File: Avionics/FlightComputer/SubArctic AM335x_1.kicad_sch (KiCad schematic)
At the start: 1 part

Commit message: Ian Goldberg - Made substantial additions to the main chip of the flight computer. Wrapping up progress for the night.
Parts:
- added R169, R170, R171, R172, R173, R35, R43, R44, R7, R9: 33R,5%, symbol Device:R
- renumbered U2 to SubArcticAM335X
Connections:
- new net MMC1_CLK: R35.2
- new net MMC1_CMD: R7.2
- new net MMC1_DAT0: R43.2
- new net MMC1_DAT1: R44.2
- new net MMC1_DAT2: R9.2
- new net MMC1_DAT3: R169.2
- new net MMC1_DAT4: R170.2
- new net MMC1_DAT5: R171.2, R172.2
- new net MMC1_DAT6: R173.2
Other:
- note added: "Are these terminated?"
- note added: "JTAG_TRSTn JTAG_TMS JTAG_TDI JTAG_TCK JTAG_TDO JTAG_EMU0 JTAG_EMU1"
- note added: "SubArctic AM335x"

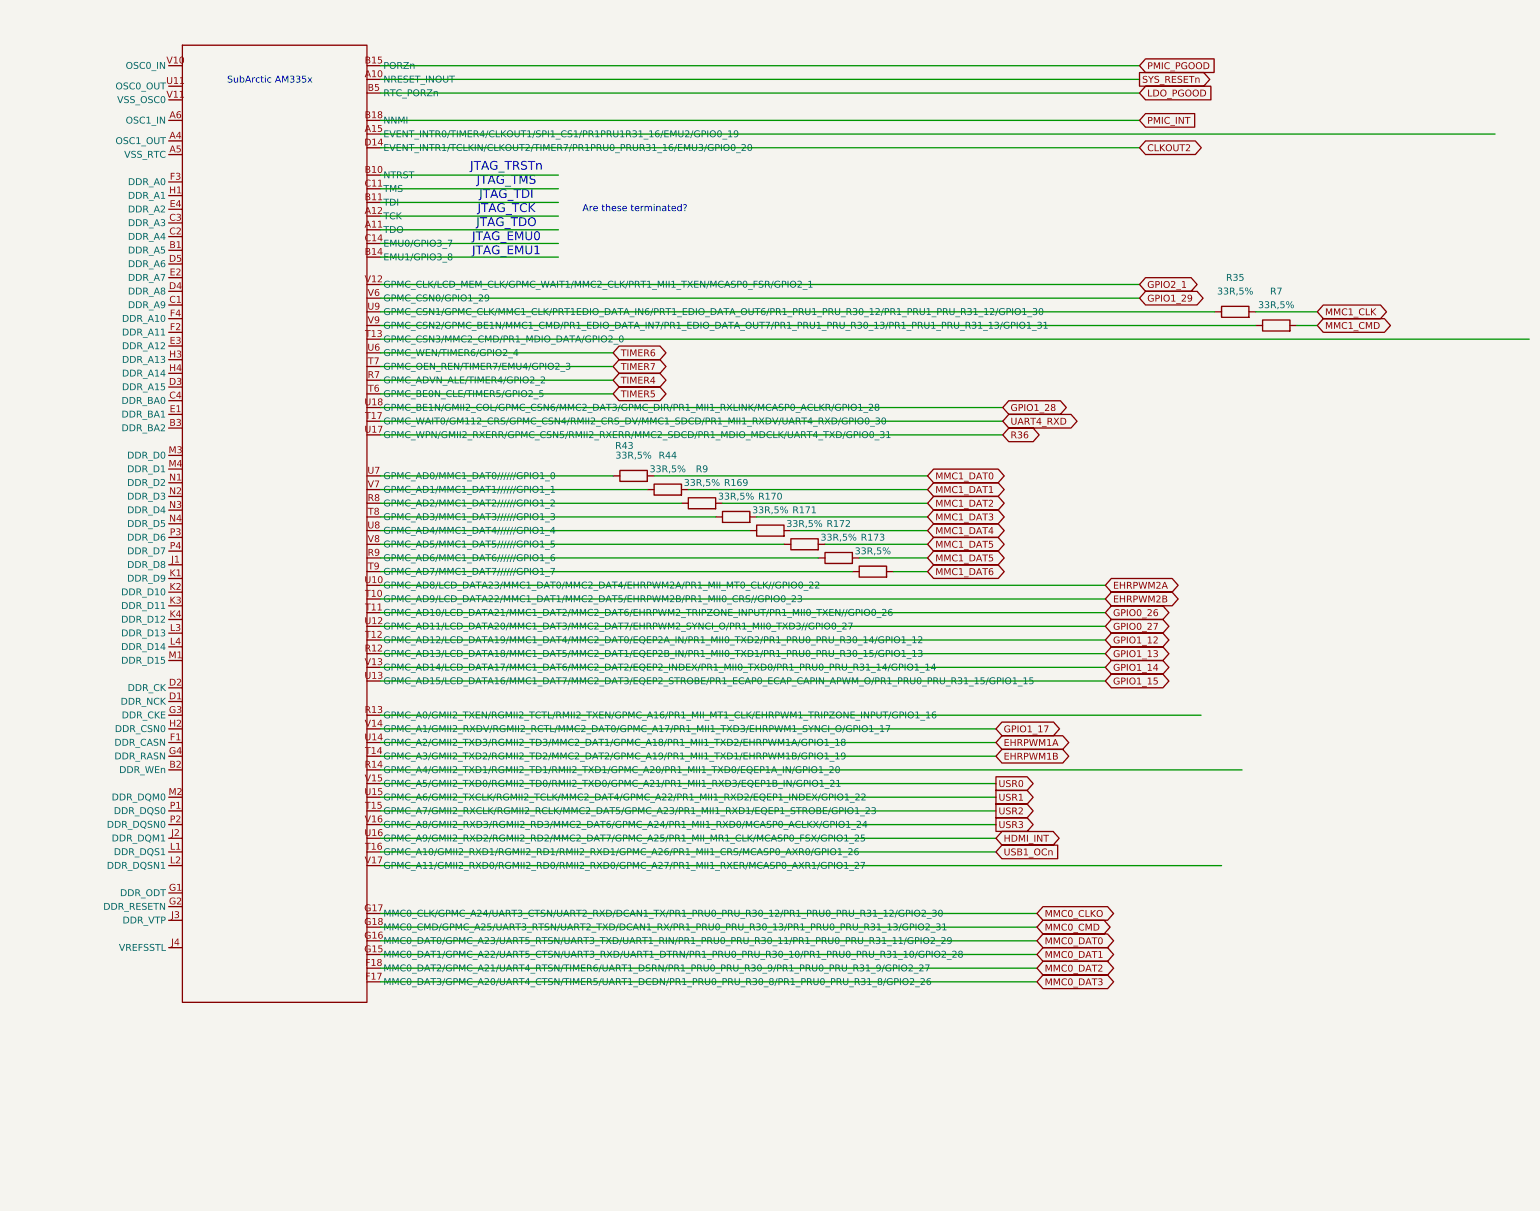
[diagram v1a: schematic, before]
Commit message: Ian Goldberg - Made more progress on the SubArctic chip pin diagram; taking ages to finish. Had a few components I added to teh Subarctic library I made, but mught want to consolidate them into a global library on my machine.
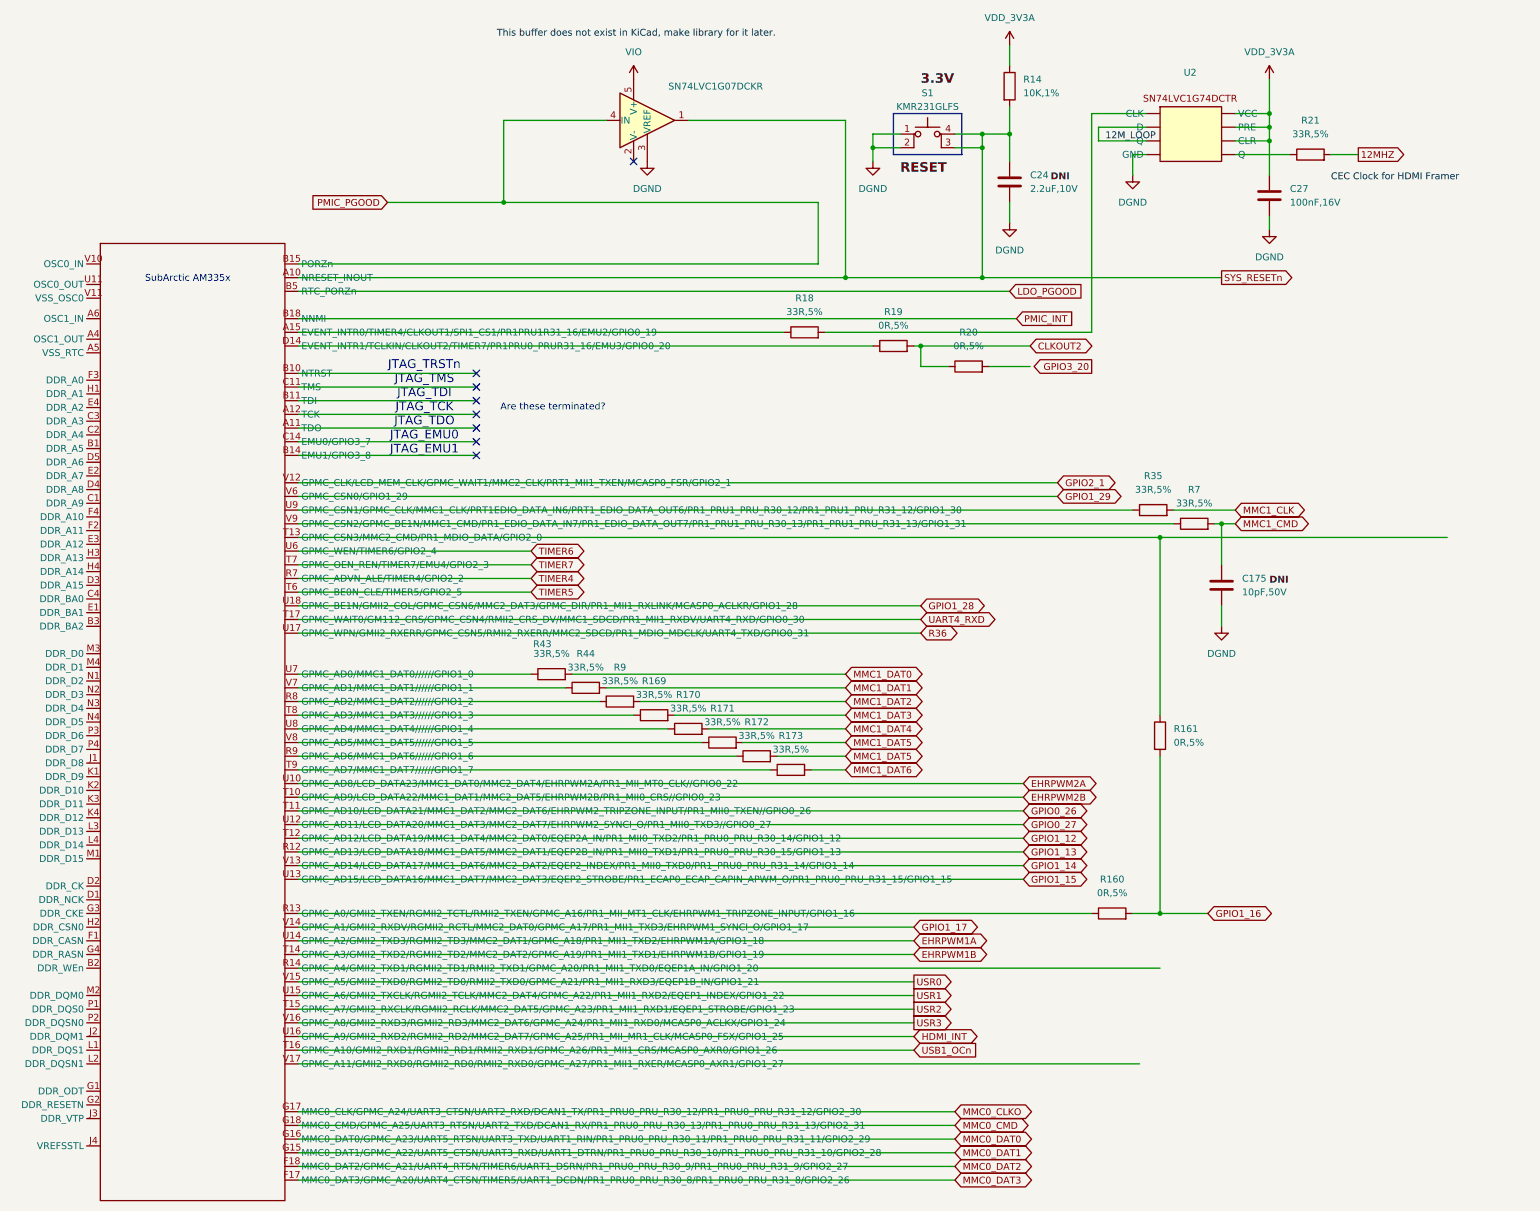
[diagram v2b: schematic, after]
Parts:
- added C175: 10pF,50V, symbol Device:C
- added C24: 2.2uF,10V, symbol Device:C
- added C27: 100nF,16V, symbol Device:C
- added R14: 10K,1%, symbol Device:R
- added R160, R161, R19, R20: 0R,5%, symbol Device:R
- added R18, R21: 33R,5%, symbol Device:R
- added S1: KMR231GLFS, symbol Switch:SW_MEC_5E
- added SN74LVC1G07DCKR: ~, Package_TO_SOT_SMD:SOT-23-5, symbol Amplifier_Buffer:BUF602xDBV
- added U2: ~, symbol SubArctic AM335x:SN74LVC1G74DCTR
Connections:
- net CLKOUT2: now also R19.2, R20.1
- net MMC1_CMD: now also C175.1
- net PMIC_PGOOD: now also SN74LVC1G07DCKR.4 (IN)
- net SYS_RESETn: now also C24.1, R14.2, S1.3 (K), S1.4 (A), SN74LVC1G07DCKR.1
- new net 12MHZ: R21.2
- new net DGND: C175.2, C24.2, C27.2, S1.1, S1.2, SN74LVC1G07DCKR.3 (VREF)
- new net GPIO1_16: R160.2, R161.2
- new net VDD_3V3A: C27.1, R14.1
- new net VIO: SN74LVC1G07DCKR.5 (V+)
- no-connect marks 0 -> 8
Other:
- title: (none) -> SubArctic AM335x Schematic #1 - Ian Goldberg
- moved on the sheet: R169, R170, R171, R172, R173, R35, R43, R44, R7, R9

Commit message: Ian Goldberg - Made more additions to the Subarctic chip
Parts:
- added C158, C159: 100nF,16V, symbol Device:C
- added R162: 0R,5%, symbol Device:R
- added R167: 33R,5%, symbol Device:R
- added SN74LVC1G07DCKR1: ~, Package_TO_SOT_SMD:SOT-23-5, symbol Amplifier_Buffer:BUF602xDBV
- added U3: ~, symbol SubArctic AM335x:ASV-24.576MHZ-E-T
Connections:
- net DGND: now also C158.2, C159.2, SN74LVC1G07DCKR1.3 (VREF)
- net VDD_3V3A: now also C158.1, SN74LVC1G07DCKR1.5 (V+)
- net VIO: now also C159.1
- new net: R162.1, SN74LVC1G07DCKR1.1
- new net GPIO3_21: R167.2
- new net eMMC_RSTn: R162.2
- no-connect marks 8 -> 9
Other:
- moved on the sheet: C175, C24, C27, R14, R160, R161, R169, R170, R171, R172, R173, R18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

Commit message: Ian Goldberg - Finished the first shceet of the Subarctic Pin-outs. Still need to make some corrections on the voltage regulator circuit but that shouldn't take too long.
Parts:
- removed SubArcticAM335X: ~, symbol SubArctic AM335x:SubArctic_AM335x
- added C21, C25, C26, C3: 18pF,50V, symbol Device:C
- added C28, C29, C30: 100nF,16V, symbol Device:C
- added R17: 1M,1%, symbol Device:R
- added R22: 49.9R,1%, symbol Device:R
- added R23, R24, R25: 4.7K,1%, symbol Device:R
- added R29, R30: 0R,5%, symbol Device:R
- added SubArcticAM335X1: ~, symbol SubArctic AM335x:SubArctic_AM335x
- added U4: ~, symbol SubArctic AM335x:JTAG_Header_2x10
- added Y1: 32.768KHz,12.5pF, symbol Device:Crystal
- added Y2: 24MHz,20pF, symbol Device:Crystal
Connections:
- net 12M_LOOP: now also U2. (VCC)
- net CLKOUT2: now also U4. (TVDD)
- net DGND: now also U2. (VCC), U3. (VCC), C28.2, C29.2, C30.2, R22.2, R25.2, R29.2, U4. (TVDD)
- net EHRPWM1A: now also SubArcticAM335X1.U14 (GPMC_A2/GMII2_TXD3/RGMII2_TD3/MMC2_DAT1/GPMC_A18/PR1_MII1_TXD2/EHRPWM1A/GPIO1_18)
- net EHRPWM1B: now also SubArcticAM335X1.T14 (GPMC_A3/GMII2_TXD2/RGMII2_TD2/MMC2_DAT2/GPMC_A19/PR1_MII1_TXD1/EHRPWM1B/GPIO1_19)
- net EHRPWM2A: now also SubArcticAM335X1.U10 (GPMC_AD8/LCD_DATA23/MMC1_DAT0/MMC2_DAT4/EHRPWM2A/PR1_MII_MT0_CLK//GPIO0_22)
- net EHRPWM2B: now also SubArcticAM335X1.T10 (GPMC_AD9/LCD_DATA22/MMC1_DAT1/MMC2_DAT5/EHRPWM2B/PR1_MII0_CRS//GPIO0_23)
- net GPIO0_26: now also SubArcticAM335X1.T11 (GPMC_AD10/LCD_DATA21/MMC1_DAT2/MMC2_DAT6/EHRPWM2_TRIPZONE_INPUT/PR1_MII0_TXEN//GPIO0_26)
- net GPIO0_27: now also SubArcticAM335X1.U12 (GPMC_AD11/LCD_DATA20/MMC1_DAT3/MMC2_DAT7/EHRPWM2_SYNCI_O/PR1_MII0_TXD3//GPIO0_27)
- net GPIO1_12: now also SubArcticAM335X1.T12 (GPMC_AD12/LCD_DATA19/MMC1_DAT4/MMC2_DAT0/EQEP2A_IN/PR1_MII0_TXD2/PR1_PRU0_PRU_R30_14/GPIO1_12)
- net GPIO1_13: now also SubArcticAM335X1.R12 (GPMC_AD13/LCD_DATA18/MMC1_DAT5/MMC2_DAT1/EQEP2B_IN/PR1_MII0_TXD1/PR1_PRU0_PRU_R30_15/GPIO1_13)
- net GPIO1_14: now also SubArcticAM335X1.V13 (GPMC_AD14/LCD_DATA17/MMC1_DAT6/MMC2_DAT2/EQEP2_INDEX/PR1_MII0_TXD0/PR1_PRU0_PRU_R31_14/GPIO1_14)
- net GPIO1_15: now also SubArcticAM335X1.U13 (GPMC_AD15/LCD_DATA16/MMC1_DAT7/MMC2_DAT3/EQEP2_STROBE/PR1_ECAP0_ECAP_CAPIN_APWM_O/PR1_PRU0_PRU_R31_15/GPIO1_15)
- net GPIO1_17: now also SubArcticAM335X1.V14 (GPMC_A1/GMII2_RXDV/RGMII2_RCTL/MMC2_DAT0/GPMC_A17/PR1_MII1_TXD3/EHRPWM1_SYNCI_O/GPIO1_17)
- net GPIO1_28: now also SubArcticAM335X1.U18 (GPMC_BE1N/GMII2_COL/GPMC_CSN6/MMC2_DAT3/GPMC_DIR/PR1_MII1_RXLINK/MCASP0_ACLKR/GPIO1_28)
- net GPIO1_29: now also SubArcticAM335X1.V6 (GPMC_CSN0/GPIO1_29)
- net GPIO2_1: now also SubArcticAM335X1.V12 (GPMC_CLK/LCD_MEM_CLK/GPMC_WAIT1/MMC2_CLK/PRT1_MII1_TXEN/MCASP0_FSR/GPIO2_1)
- net HDMI_INT: now also SubArcticAM335X1.U16 (GPMC_A9/GMII2_RXD2/RGMII2_RD2/MMC2_DAT7/GPMC_A25/PR1_MII_MR1_CLK/MCASP0_FSX/GPIO1_25)
- net LDO_PGOOD: now also SubArcticAM335X1.B5 (RTC_PORZn)
- net MMC0_CLKO: now also SubArcticAM335X1.G17 (MMC0_CLK/GPMC_A24/UART3_CTSN/UART2_RXD/DCAN1_TX/PR1_PRU0_PRU_R30_12/PR1_PRU0_PRU_R31_12/GPIO2_30)
- net MMC0_CMD: now also SubArcticAM335X1.G18 (MMC0_CMD/GPMC_A25/UART3_RTSN/UART2_TXD/DCAN1_RX/PR1_PRU0_PRU_R30_13/PR1_PRU0_PRU_R31_13/GPIO2_31)
- net MMC0_DAT0: now also SubArcticAM335X1.G16 (MMC0_DAT0/GPMC_A23/UART5_RTSN/UART3_TXD/UART1_RIN/PR1_PRU0_PRU_R30_11/PR1_PRU0_PRU_R31_11/GPIO2_29)
- net MMC0_DAT1: now also SubArcticAM335X1.G15 (MMC0_DAT1/GPMC_A22/UART5_CTSN/UART3_RXD/UART1_DTRN/PR1_PRU0_PRU_R30_10/PR1_PRU0_PRU_R31_10/GPIO2_28)
- net MMC0_DAT2: now also SubArcticAM335X1.F18 (MMC0_DAT2/GPMC_A21/UART4_RTSN/TIMER6/UART1_DSRN/PR1_PRU0_PRU_R30_9/PR1_PRU0_PRU_R31_9/GPIO2_27)
- net MMC0_DAT3: now also SubArcticAM335X1.F17 (MMC0_DAT3/GPMC_A20/UART4_CTSN/TIMER5/UART1_DCDN/PR1_PRU0_PRU_R30_8/PR1_PRU0_PRU_R31_8/GPIO2_26)
- net PMIC_INT: now also SubArcticAM335X1.B18 (NNMI)
- net PMIC_PGOOD: now also SubArcticAM335X1.B15 (PORZn)
- net R36: now also SubArcticAM335X1.U17 (GPMC_WPN/GMII2_RXERR/GPMC_CSN5/RMII2_RXERR/MMC2_SDCD/PR1_MDIO_MDCLK/UART4_TXD/GPIO0_31)
- net SYS_RESETn: now also SubArcticAM335X1.A10 (NRESET_INOUT)
- net TIMER4: now also SubArcticAM335X1.R7 (GPMC_ADVN_ALE/TIMER4/GPIO2_2)
- net TIMER5: now also SubArcticAM335X1.T6 (GPMC_BE0N_CLE/TIMER5/GPIO2_5)
- net TIMER6: now also SubArcticAM335X1.U6 (GPMC_WEN/TIMER6/GPIO2_4)
- net TIMER7: now also SubArcticAM335X1.T7 (GPMC_OEN_REN/TIMER7/EMU4/GPIO2_3)
- net UART4_RXD: now also SubArcticAM335X1.T17 (GPMC_WAIT0/GM112_CRS/GPMC_CSN4/RMII2_CRS_DV/MMC1_SDCD/PR1_MII1_RXDV/UART4_RXD/GPIO0_30)
- net USB1_OCn: now also SubArcticAM335X1.T16 (GPMC_A10/GMII2_RXD1/RGMII2_RD1/RMII2_RXD1/GPMC_A26/PR1_MII1_CRS/MCASP0_AXR0/GPIO1_26)
- net USR0: now also SubArcticAM335X1.V15 (GPMC_A5/GMII2_TXD0/RGMII2_TD0/RMII2_TXD0/GPMC_A21/PR1_MII1_RXD3/EQEP1B_IN/GPIO1_21)
- net USR1: now also SubArcticAM335X1.U15 (GPMC_A6/GMII2_TXCLK/RGMII2_TCLK/MMC2_DAT4/GPMC_A22/PR1_MII1_RXD2/EQEP1_INDEX/GPIO1_22)
- net USR2: now also SubArcticAM335X1.T15 (GPMC_A7/GMII2_RXCLK/RGMII2_RCLK/MMC2_DAT5/GPMC_A23/PR1_MII1_RXD1/EQEP1_STROBE/GPIO1_23)
- net USR3: now also SubArcticAM335X1.V16 (GPMC_A8/GMII2_RXD3/RGMII2_RD3/MMC2_DAT6/GPMC_A24/PR1_MII1_RXD0/MCASP0_ACLKX/GPIO1_24)
- net VDD_3V3A: now also U2. (VCC)
- net VIO: now also U3. (VCC)
- net at R172.1: now also SubArcticAM335X1.R9 (GPMC_AD6/MMC1_DAT6//////GPIO1_6)
- net at R35.1: now also SubArcticAM335X1.U9 (GPMC_CSN1/GPMC_CLK/MMC1_CLK/PRT1EDIO_DATA_IN6/PRT1_EDIO_DATA_OUT6/PR1_PRU1_PRU_R30_12/PR1_PRU1_PRU_R31_12/GPIO1_30)
- net at R173.1: now also SubArcticAM335X1.T9 (GPMC_AD7/MMC1_DAT7//////GPIO1_7)
- net at SN74LVC1G07DCKR1.4 (IN): now also SubArcticAM335X1.R14 (GPMC_A4/GMII2_TXD1/RGMII2_TD1/RMII2_TXD1/GPMC_A20/PR1_MII1_TXD0/EQEP1A_IN/GPIO1_20)
- net at R160.1: now also SubArcticAM335X1.R13 (GPMC_A0/GMII2_TXEN/RGMII2_TCTL/RMII2_TXEN/GPMC_A16/PR1_MII_MT1_CLK/EHRPWM1_TRIPZONE_INPUT/GPIO1_16)
- net at R171.1: now also SubArcticAM335X1.V8 (GPMC_AD5/MMC1_DAT5//////GPIO1_5)
- net at R9.1: now also SubArcticAM335X1.R8 (GPMC_AD2/MMC1_DAT2//////GPIO1_2)
- net at R170.1: now also SubArcticAM335X1.U8 (GPMC_AD4/MMC1_DAT4//////GPIO1_4)
- net at R18.1: now also SubArcticAM335X1.A15 (EVENT_INTR0/TIMER4/CLKOUT1/SPI1_CS1/PR1PRU1R31_16/EMU2/GPIO0_19)
- net at R18.2: now also U2. (VCC)
- net at R44.1: now also SubArcticAM335X1.V7 (GPMC_AD1/MMC1_DAT1//////GPIO1_1)
- net at R19.1: now also SubArcticAM335X1.D14 (EVENT_INTR1/TCLKIN/CLKOUT2/TIMER7/PR1PRU0_PRUR31_16/EMU3/GPIO0_20)
- net at R169.1: now also SubArcticAM335X1.T8 (GPMC_AD3/MMC1_DAT3//////GPIO1_3)
- net at R161.1: now also SubArcticAM335X1.T13 (GPMC_CSN3/MMC2_CMD/PR1_MDIO_DATA/GPIO2_0)
- net at R43.1: now also SubArcticAM335X1.U7 (GPMC_AD0/MMC1_DAT0//////GPIO1_0)
- net at R167.1: now also U3. (VCC)
- net at R7.1: now also SubArcticAM335X1.V9 (GPMC_CSN2/GPMC_BE1N/MMC1_CMD/PR1_EDIO_DATA_IN7/PR1_EDIO_DATA_OUT7/PR1_PRU1_PRU_R30_13/PR1_PRU1_PRU_R31_13/GPIO1_31)
- net at R21.1: now also U2. (VCC)
- new net: C30.1, U4. (TVDD)
- new net: C21.1, C3.1, R30.2, SubArcticAM335X1.A5 (VSS_RTC)
- new net: C21.2, SubArcticAM335X1.A6 (OSC1_IN), Y1.2
- new net: C3.2, SubArcticAM335X1.A4 (OSC1_OUT), Y1.1
- new net: R22.1, SubArcticAM335X1.J3 (DDR_VTP)
- new net: C26.1, R17.2, SubArcticAM335X1.U11 (OSC0_OUT), Y2.1
- new net: C25.1, R17.1, SubArcticAM335X1.V10 (OSC0_IN), Y2.2
- new net: SubArcticAM335X1.V17 (GPMC_A11/GMII2_RXD0/RGMII2_RD0/RMII2_RXD0/GPMC_A27/PR1_MII1_RXER/MCASP0_AXR1/GPIO1_27), U3. (VCC)
- new net: R23.2, U4. (TVDD)
- new net: R25.1, U4. (TVDD)
- new net: R24.1, U4. (TVDD)
- new net DDR_CASn: SubArcticAM335X1.F1 (DDR_CASN)
- new net DDR_CKE: SubArcticAM335X1.G3 (DDR_CKE)
- new net DDR_CLK: SubArcticAM335X1.D2 (DDR_CK)
- new net DDR_CLKn: SubArcticAM335X1.D1 (DDR_NCK)
- new net DDR_CSn: SubArcticAM335X1.H2 (DDR_CSN0)
- new net DDR_DQM0: SubArcticAM335X1.M2 (DDR_DQM0)
- new net DDR_DQM1: SubArcticAM335X1.J2 (DDR_DQM1)
- new net DDR_DQS0: SubArcticAM335X1.P1 (DDR_DQS0)
- new net DDR_DQS1: SubArcticAM335X1.L1 (DDR_DQS1)
- new net DDR_DQSN0: SubArcticAM335X1.P2 (DDR_DQSN0)
- new net DDR_DQSN1: SubArcticAM335X1.L2 (DDR_DQSN1)
- new net DDR_ODT: SubArcticAM335X1.G1 (DDR_ODT)
- new net DDR_RASn: SubArcticAM335X1.G4 (DDR_RASN)
- new net DDR_RESETn: SubArcticAM335X1.G2 (DDR_RESETN)
- new net DDR_VREF: C28.1, SubArcticAM335X1.J4 (VREFSSTL)
- new net DDR_WEn: SubArcticAM335X1.B2 (DDR_WEn)
- new net GND_OSC0: C25.2, C26.2, R29.1, R30.1, SubArcticAM335X1.V11 (VSS_OSC0)
- new net MMC0_CD: U4. (TVDD)
- new net VDD_3V3B: C29.1, R23.1, R24.2, U4. (TVDD)
- no-connect marks 9 -> 14
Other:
- note removed: "SubArctic AM335x"
- moved on the sheet: C158, C159, C175, C24, C27, R14, R160, R161, R162, R167, R169, R170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

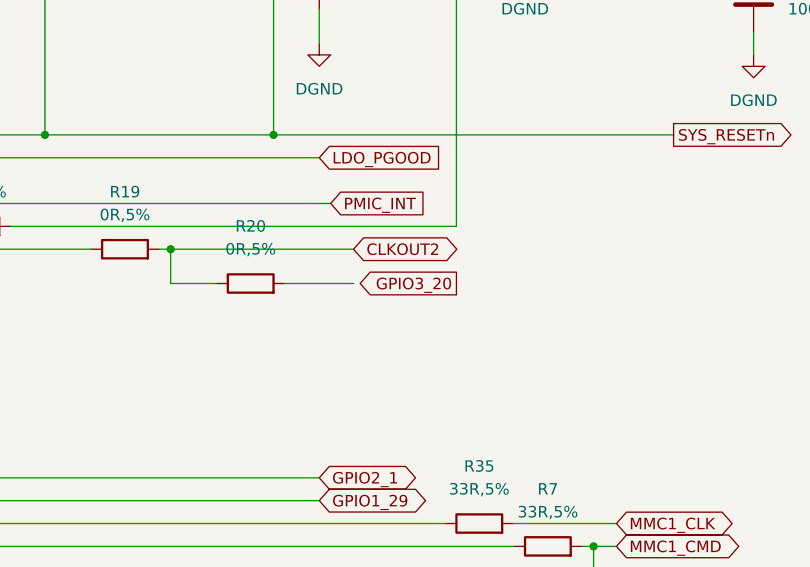
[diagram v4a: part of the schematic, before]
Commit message: Ian Goldberg - Finished sheet no. 1 of the beagleboard and am on to sheet no. 2
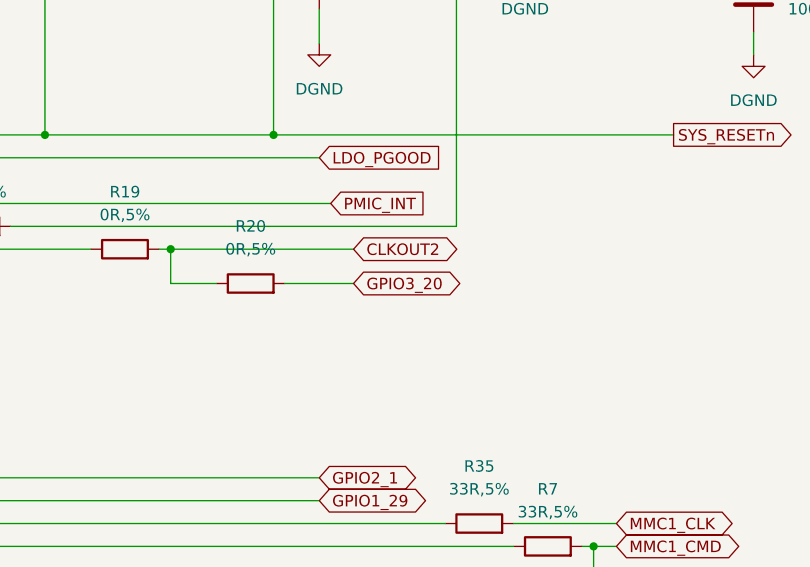
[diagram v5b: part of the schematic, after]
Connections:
- net GPIO3_20: now also R20.2
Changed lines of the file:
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@@
 	)
 	(global_label "GPIO3_20"
-		(shape output)
-		(at 429.26 83.82 180)
+		(shape bidirectional)
+		(at 417.83 83.82 0)
 		(fields_autoplaced yes)
 		(effects
@@
 				(size 1.27 1.27)
 			)
-			(justify right)
+			(justify left)
 		)
 		(property "Intersheetrefs" "${INTERSHEET_REFS}"
-			(at 417.2034 83.82 0)
+			(at 430.9979 83.82 0)
 			(effects
 				(font
 					(size 1.27 1.27)
 				)
-				(justify right)
+				(justify left)
 				(hide yes)
 			)

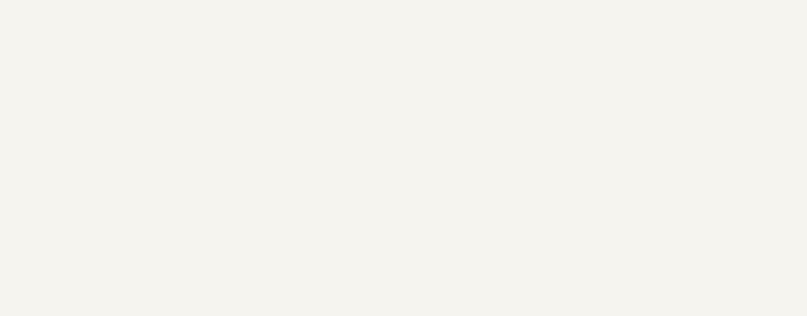
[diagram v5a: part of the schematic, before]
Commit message: Ian Goldberg - Finished the second pin diagram for the SubArctic AM335x chip - only one more to go after this one.
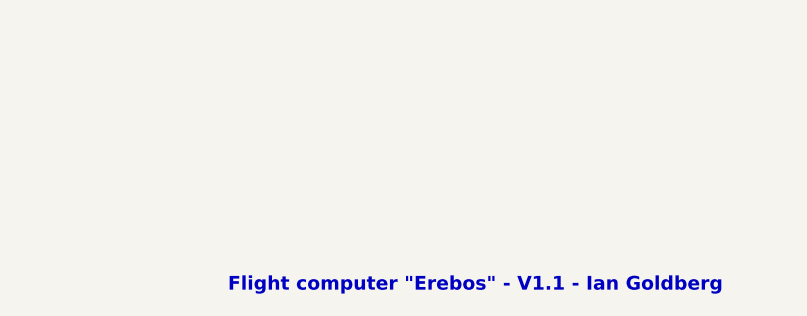
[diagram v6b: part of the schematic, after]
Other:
- note added: "Flight computer "Erebos" - V1.1 - Ian Goldberg"
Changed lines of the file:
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@@
+		)
+	)
+	(text "Flight computer \"Erebos\" - V1.1 - Ian Goldberg\n\n"
+		(exclude_from_sim no)
+		(at 503.682 379.73 0)
+		(effects
+			(font
+				(size 1.524 1.524)
+				(thickness 0.254)
+				(bold yes)
+			)
 		)
 	)

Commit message: Ian Goldberg - Finished the pin-out for the third schematic of the SubArctic chip. All that remains is finishing up the rest of the circuit.
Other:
- note added: "Flight computer - V1.1 - Ian Goldberg"
- note removed: "Flight computer "Erebos" - V1.1 - Ian Goldberg"
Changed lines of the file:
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@@
 		)
 	)
-	(text "Flight computer \"Erebos\" - V1.1 - Ian Goldberg\n\n"
+	(text "Flight computer - V1.1 - Ian Goldberg\n\n"
 		(exclude_from_sim no)
 		(at 503.682 379.73 0)
@@
 				(bold yes)
 			)
-			(justify left bottom)
-		)
-	)
-	(label "SubArctic AM335x"
-		(at 158.75 71.12 0)
-		(fields_autoplaced yes)
-		(effects
-			(font
-				(size 3.048 3.048)
-				(thickness 0.6096)
-				(bold yes)
-			)
